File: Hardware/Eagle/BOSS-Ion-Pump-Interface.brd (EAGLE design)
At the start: 48.3 x 66 mm, 27 parts, among them J4 PINHD-1X2-MOLEX-22112022, U1 ISO224ADWVR, U2 ISO224ADWVR

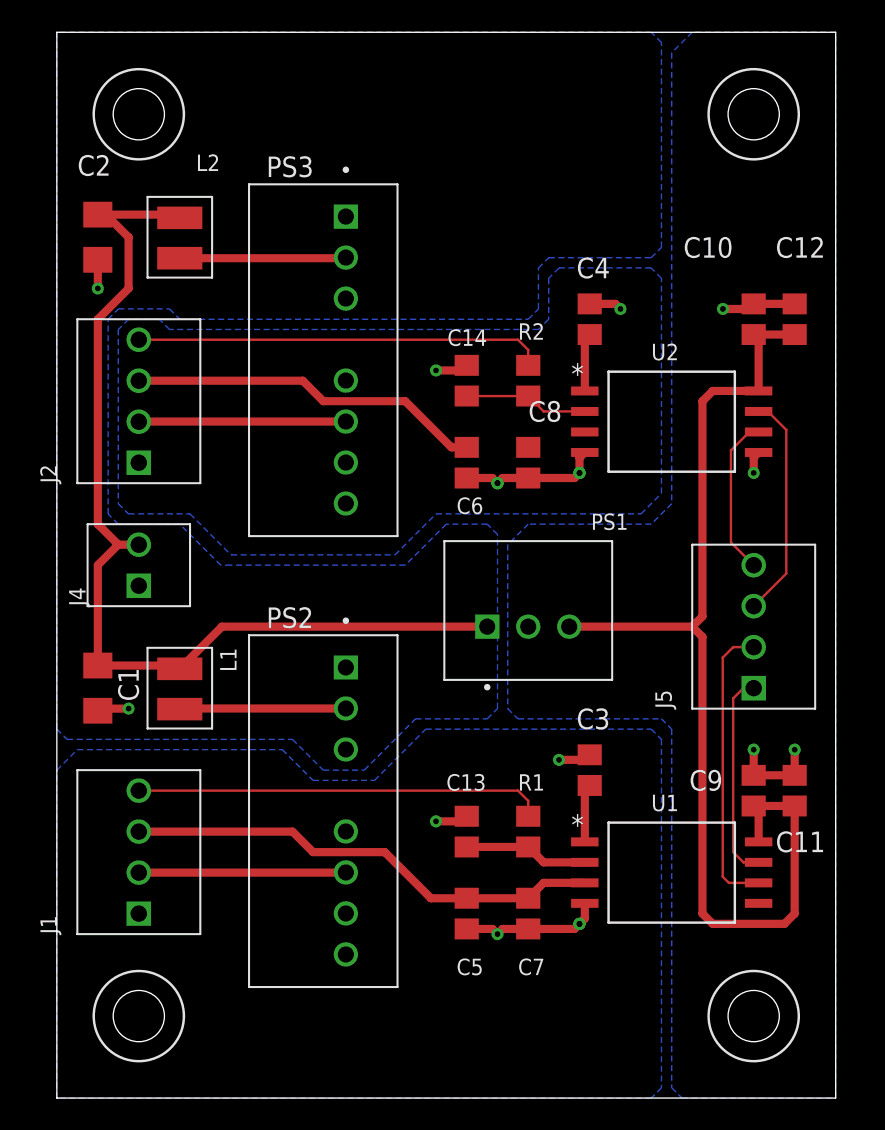
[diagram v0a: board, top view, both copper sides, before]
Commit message: Increased capacitor voltages and changed to 1206
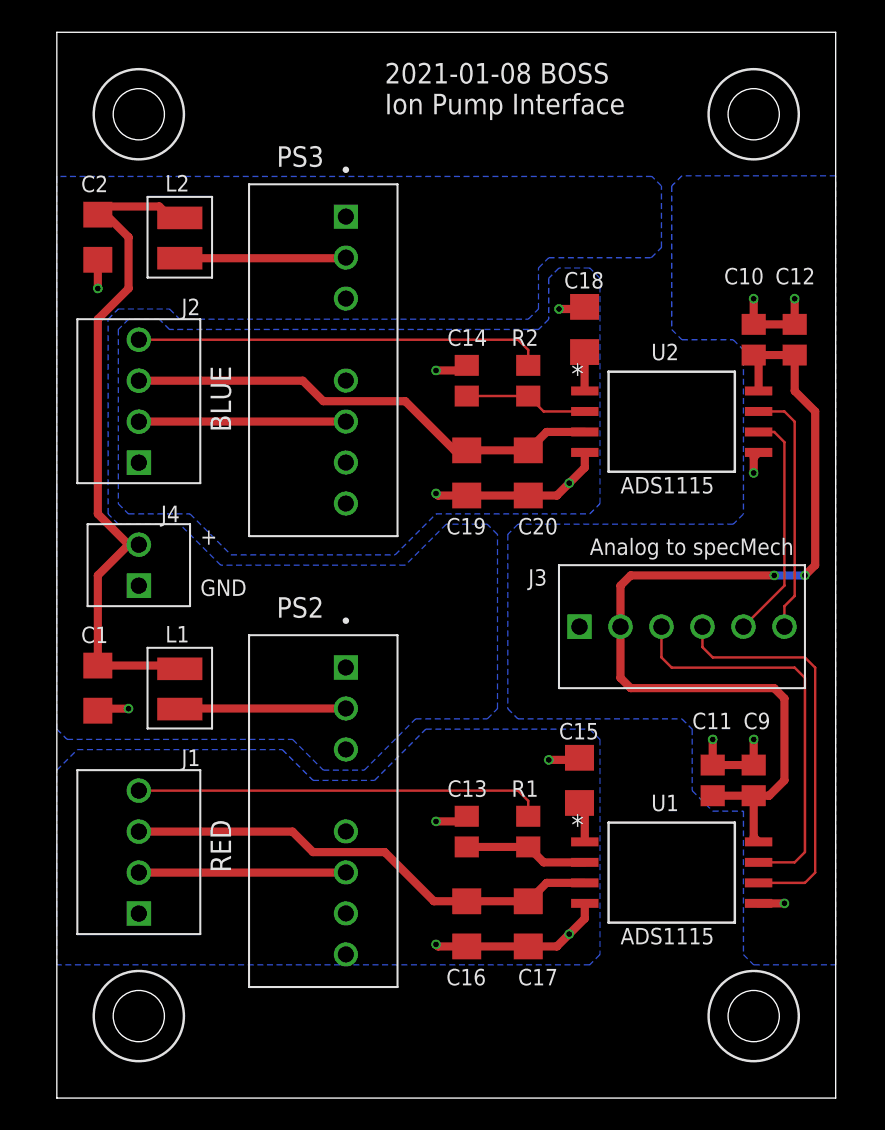
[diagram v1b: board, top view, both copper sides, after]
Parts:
- removed C3, C4: 0.22uF, AUmlib:C0805
- removed C5, C6: 1uF, AUmlib:C0805
- removed C7, C8: 0.1uF, AUmlib:C0805
- removed J5: (no value), AUmlib:1X04-MOLEX-22112042
- removed PS1: OKI-78SR-5/1.5-W36-C, AUmlib:CONV_OKI-78SR-5/1.5-W36-C
- added C15, C18: 0.22uF, AUmlib:C1206
- added C16, C19: 1uF, AUmlib:C1206
- added C17, C20: .1uF, AUmlib:C1206
- added J3: MOLEX-22112062, AUmlib:1X06-MOLEX-22112062
- C13, C14: value 0.1uF -> 1.0uF
- J1, J2: value (none) -> MOLEX-22112042
- J4: value PINHD-1X2-MOLEX-22112022 -> MOLEX-22112022
- R1, R2: value (none) -> 1K
- moved C11 5.12 mm to (40.6, 19.7)
- moved C10 1.27 mm to (43.2, 47.0)
- moved C12 1.27 mm to (45.7, 47.0)
- moved C9 0.63 mm to (43.2, 19.7)
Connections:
- removed net GND-ISO-1: C13.2, C3.2, C5.2, C7.2, J1.1, PS2.7, U1.4
- removed net GND-ISO-2: C14.2, C4.2, C6.2, C8.2, J2.1, PS3.7, U2.4
- new net GND-ISO-BLU: C14.2, C18.2, C19.2, C20.2, J2.1, PS3.7, U2.4
- new net GND-ISO-RED: C13.2, C15.2, C16.2, C17.2, J1.1, PS2.7, U1.4
- net +24V: no longer PS1.1
- net +5V: now also J3.2; no longer PS1.3
- net BLUE+: now also J3.6; no longer J5.3
- net BLUE-: now also J3.5; no longer J5.4
- net GND: now also J3.1; no longer PS1.2
- net N$2: now also C15.1; no longer C3.1
- net N$6: now also C18.1; no longer C4.1
- net RED+: now also J3.3; no longer J5.1
- net RED-: now also J3.4; no longer J5.2
- net VDD1-BLUE: now also C19.1, C20.1; no longer C6.1, C8.1
- net VDD1-RED: now also C16.1, C17.1; no longer C5.1, C7.1
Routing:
- net +24V: track 62.6 -> 42.8 mm
- net GND-ISO-RED: track 0.00 -> 14.9 mm, vias 0 -> 4
- net GND-ISO-BLU: track 0.00 -> 14.6 mm, vias 0 -> 4
- net GND-ISO-1: track 12.9 -> 0.00 mm, vias 5 -> 0
- net GND-ISO-2: track 12.9 -> 0.00 mm, vias 6 -> 0
- net RED+: track 13.5 -> 25.2 mm
- net VDD1-BLUE: track 22.0 -> 29.9 mm
- net +5V: track 67.6 -> 60.3 mm, vias 0 -> 2
- net RED-: track 18.1 -> 25.2 mm
- net BLUE-: track 9.88 -> 14.3 mm
- net GND: track 11.7 -> 14.4 mm, vias 4 -> 6
- net BLUE+: track 13.9 -> 15.5 mm
- net N$6: track 3.62 -> 2.42 mm
- net N$2: track 3.62 -> 2.55 mm
- added copper zone on layer 16, net GND-ISO-BLU
- added copper zone on layer 16, net GND-ISO-RED
- removed copper zone on layer 16, net GND-ISO-1
- removed copper zone on layer 16, net GND-ISO-2
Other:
- board text added: "+"
- board text added: "+15V"
- board text added: "+5V"
- board text added: "2021-01-08 BOSS Ion Pump Interface"
- board text added: "ADS1115"
- board text added: "Analog to specMech"
- board text added: "BLUE"
- board text added: "BLUE+"
- board text added: "BLUE-"
- board text added: "GND"
- board text added: "GND-ISO-BLU"
- board text added: "GND-ISO-RED"
- board text added: "RED"
- board text added: "RED+"
- board text added: "RED-"

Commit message: Added test points, cleaned up ERC check
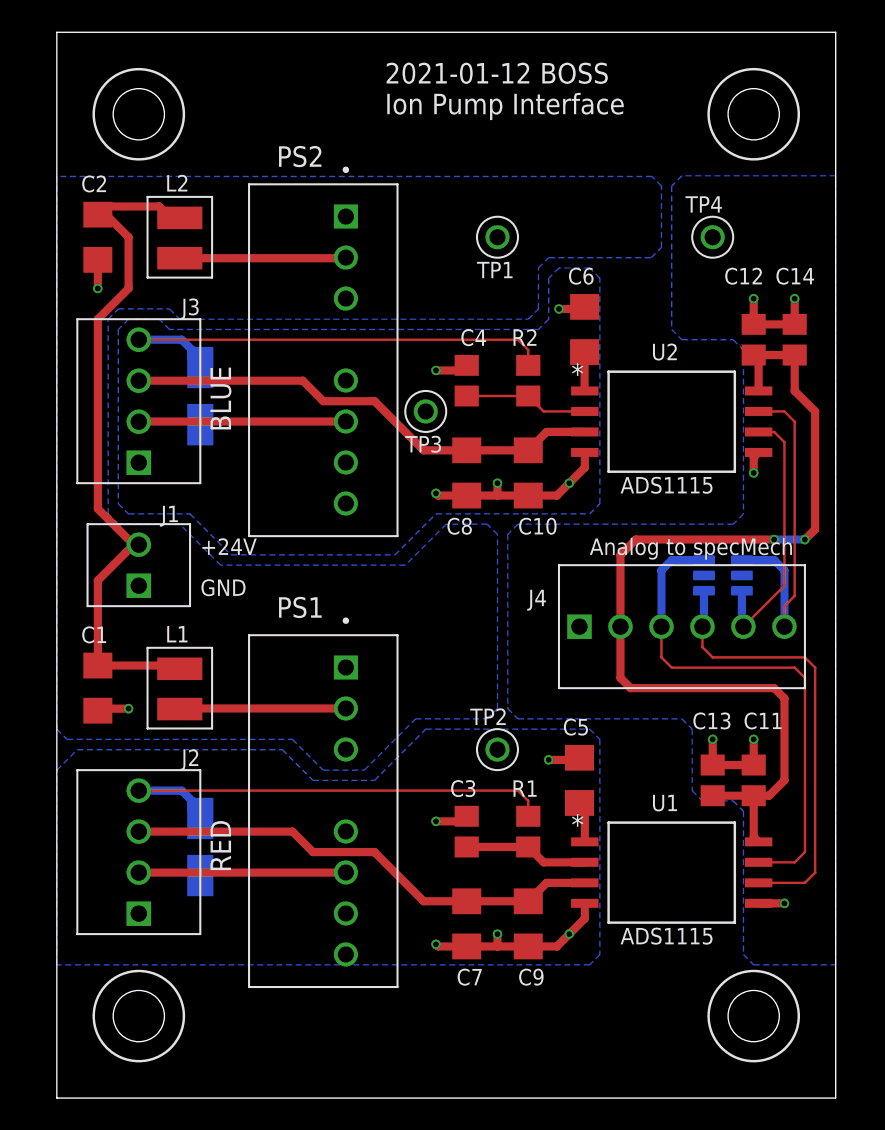
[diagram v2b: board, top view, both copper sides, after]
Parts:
- removed C17, C20: .1uF, AUmlib:C1206
- removed PS3: RECOM-RS6-2415S, AUmlib:CONV_RS6-2415S
- added C3, C4: 1.0uF, AUmlib:C0805
- added PS1: RECOM-RS6-2415S, AUmlib:CONV_RS6-2415S
- added TP1, TP2, TP3, TP4: TP5000-TESTPOINT-BLK, AUmlib:TP5000-TESTPOINT-BLK
- added TVS1, TVS2: SMAJ6.0CA-13F, AUmlib:SMA_DIO-M
- added TVS3: ESDA6V1BC6, AUmlib:SOT95P280X145-6N
- C10, C9: device AUmlib:C0805 -> AUmlib:C1206
- C11, C12: value 1uF -> 0.1uF
- C13, C14: value 1.0uF -> 1uF
- C7, C8: value 1uF -> 1.0uF
- J1: value MOLEX-22112042 -> MOLEX-22112022; device AUmlib:1X04-MOLEX-22112042 -> AUmlib:1X02-MOLEX-22112022
- J3: value MOLEX-22112062 -> MOLEX-22112042; device AUmlib:1X06-MOLEX-22112062 -> AUmlib:1X04-MOLEX-22112042
- J4: value MOLEX-22112022 -> MOLEX-22112062; device AUmlib:1X02-MOLEX-22112022 -> AUmlib:1X06-MOLEX-22112062
- moved J3 33.9 mm to (5.08, 39.4), turned to 90 degrees
- moved J4 32.6 mm to (37.5, 29.2), turned to 0 degrees
- moved J2 27.9 mm to (5.08, 11.4)
- moved PS2 27.9 mm to (16.5, 45.7)
- moved J1 21.6 mm to (5.08, 33.0)
- moved C14 20.5 mm to (45.7, 47.0)
- moved C9 16.6 mm to (29.2, 10.8), turned to 270 degrees
- moved C10 16.2 mm to (29.2, 38.7), turned to 270 degrees
- moved C13 15.6 mm to (40.6, 19.7)
- moved C11 2.54 mm to (43.2, 19.7)
- moved C12 2.54 mm to (43.2, 47.0)
- renumbered C15 to C5, C16 to C7, C18 to C6, C19 to C8
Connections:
- net N$2 renamed VCAP-RED
- net N$6 renamed VCAP-BLUE
- removed net BLUE+: J3.6, U2.7
- removed net BLUE-: J3.5, U2.6
- removed net GND-ISO-BLU: C14.2, C20.2, C6.2, C8.2, J2.1, PS3.7, U2.4
- removed net N$14: J2.4, R2.1
- removed net N$4: L1.2, PS2.2
- removed net N$5: J1.4, R1.1
- removed net N$9: L2.2, PS3.2
- removed net RED+: J3.3, U1.7
- removed net RED-: J3.4, U1.6
- new net +VIN-BLUE: L2.2, PS2.2
- new net +VIN-RED: L1.2, PS1.2
- new net FROM-BLUE-PUMP: J3.4, R2.1, TVS2.1
- new net FROM-RED-PUMP: J2.4, R1.1, TVS1.1
- new net GND-ISO-BLUE: C10.2, C4.2, C6.2, C8.2, J3.1, PS2.7, TP3.P$1, TVS2.2, U2.4
- new net OUTN-BLUE: J4.5, TVS3.3, U2.6
- new net OUTN-RED: J4.4, TVS3.4, U1.6
- new net OUTP-BLUE: J4.6, TVS3.1, U2.7
- new net OUTP-RED: J4.3, TVS3.6, U1.7
- net +15V-BLUE: now also J3.2, PS2.6; no longer J2.2, PS3.6
- net +15V-RED: now also J2.2, PS1.6; no longer J1.2, PS2.6
- net +24V: now also J1.2; no longer J4.2
- net +5V: now also C13.1, C14.1, J4.2; no longer C10.1, C9.1, J3.2
- net GND: now also C13.2, C14.2, J4.1, TP4.P$1, TVS3.2, TVS3.5; no longer C10.2, C9.2, J3.1
- net GND-1: now also J1.1, PS1.1, TP1.P$1; no longer J4.1, PS3.1
- net GND-ISO-RED: now also C3.2, C9.2, J2.1, PS1.7, TP2.P$1, TVS1.2; no longer C13.2, C17.2, J1.1, PS2.7
- net IN-BLUE: now also C4.1; no longer C14.1
- net IN-RED: now also C3.1; no longer C13.1
- net VDD1-BLUE: now also C10.1, J3.3; no longer C20.1, J2.3
- net VDD1-RED: now also C9.1, J2.3; no longer C17.1, J1.3
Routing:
- net OUTP-RED: track 0.00 -> 31.6 mm
- net FROM-BLUE-PUMP: track 0.00 -> 30.2 mm
- net FROM-RED-PUMP: track 0.00 -> 30.2 mm
- net OUTN-RED: track 0.00 -> 27.5 mm
- net N$14: track 25.3 -> 0.00 mm
- net N$5: track 25.3 -> 0.00 mm
- net RED-: track 25.2 -> 0.00 mm
- net RED+: track 25.2 -> 0.00 mm
- net OUTP-BLUE: track 0.00 -> 21.9 mm
- net OUTN-BLUE: track 0.00 -> 16.6 mm
- net BLUE+: track 15.5 -> 0.00 mm
- net GND-ISO-BLUE: track 0.00 -> 15.4 mm, vias 0 -> 5
- net GND-ISO-BLU: track 14.6 -> 0.00 mm, vias 4 -> 0
- net BLUE-: track 14.3 -> 0.00 mm
- net N$4: track 10.3 -> 0.00 mm
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- added copper zone on layer 16, net GND-ISO-BLUE
- removed copper zone on layer 16, net GND-ISO-BLU
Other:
- board text added: "+24V"
- board text added: "2021-01-12 BOSS Ion Pump Interface"
- board text removed: "+"
- board text removed: "2021-01-08 BOSS Ion Pump Interface"
- board text removed: "GND-ISO-BLU"
- board text removed: "GND-ISO-RED"

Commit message: Added external parts (switches and panel connectors)
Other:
- board text added: "2021-01-13 BOSS Ion Pump Interface"
- board text removed: "2021-01-12 BOSS Ion Pump Interface"
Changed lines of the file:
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@@
 <hole x="43.18" y="60.96" drill="3.175"/>
 <circle x="43.18" y="60.96" radius="2.794" width="0.1524" layer="21"/>
-<text x="20.32" y="60.96" size="1.27" layer="21">2021-01-12 BOSS
+<text x="20.32" y="60.96" size="1.27" layer="21">2021-01-13 BOSS
 Ion Pump Interface</text>
 <text x="41.91" y="23.495" size="1.016" layer="22" font="vector" rot="MR90">BLUE-</text>
@@
 <text x="16.51" y="41.275" size="1.016" layer="22" font="vector" rot="MR0">+15V</text>
 <text x="16.51" y="13.335" size="1.016" layer="22" font="vector" rot="MR0">+15V</text>
-<text x="34.29" y="60.96" size="1.27" layer="22" rot="MR0">2021-01-12 BOSS
+<text x="34.29" y="60.96" size="1.27" layer="22" rot="MR0">2021-01-13 BOSS
 Ion Pump Interface</text>
 </plain>
